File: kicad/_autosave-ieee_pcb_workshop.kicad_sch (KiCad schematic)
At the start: 42 parts, among them J1 Conn_01x10, J2 Conn_01x10, J3 ICSP, J4 USB_B_Micro, U1 ATmega32U4-A, Y1 16MHz

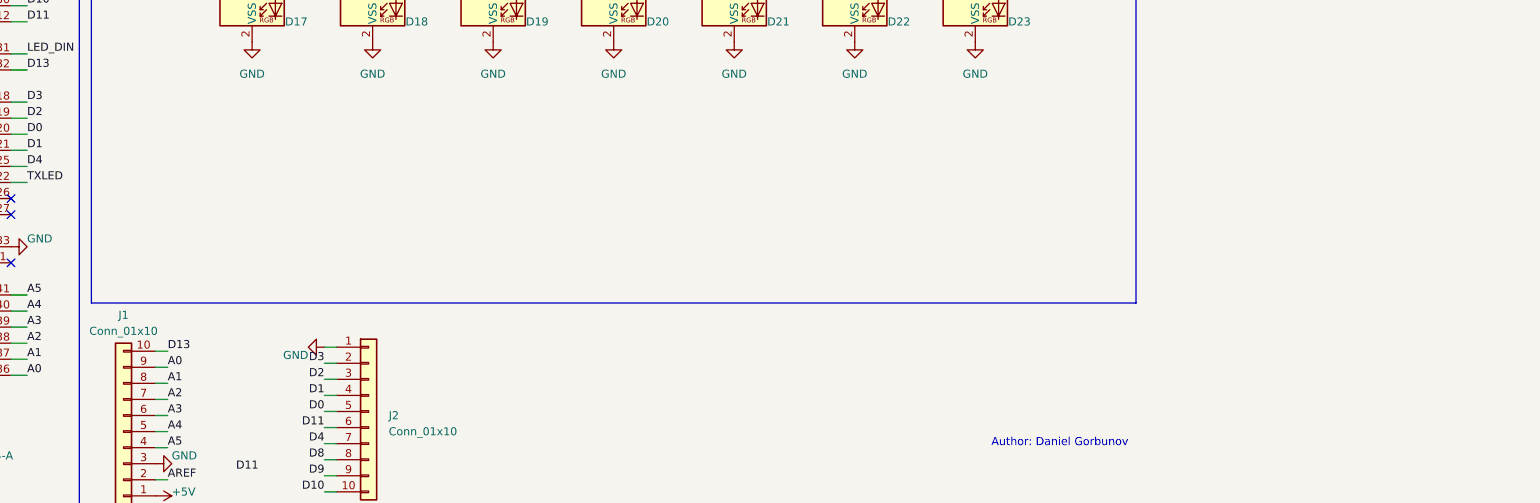
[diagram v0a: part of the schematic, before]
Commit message: add lecture 2
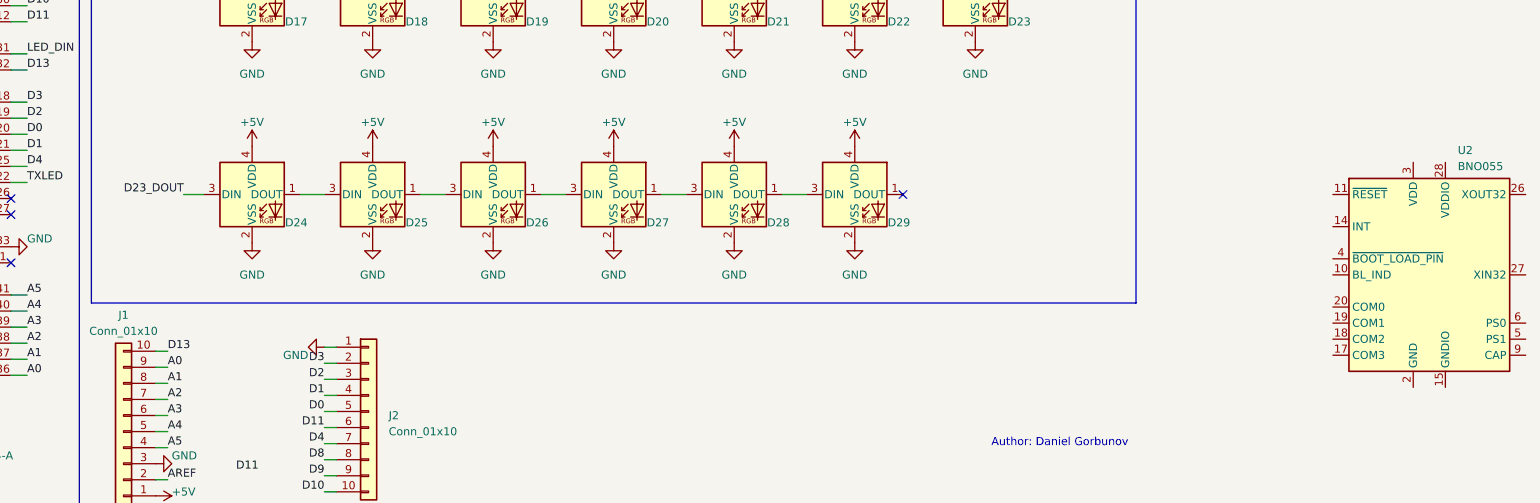
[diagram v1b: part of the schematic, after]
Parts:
- added D24, D25, D26, D27, D28, D29: SK6812MINI, LED_SMD:LED_SK6812MINI_PLCC4_3.5x3.5mm_P1.75mm, symbol LED:SK6812MINI
- added U2: BNO055, Package_LGA:LGA-28_5.2x3.8mm_P0.5mm, symbol Sensor_Motion:BNO055
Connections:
- net +5V: now also D24.4 (VDD), D25.4 (VDD), D26.4 (VDD), D27.4 (VDD), D28.4 (VDD), D29.4 (VDD)
- net D23_DOUT: now also D24.3 (DIN)
- net GND: now also D24.2 (VSS), D25.2 (VSS), D26.2 (VSS), D27.2 (VSS), D28.2 (VSS), D29.2 (VSS)
- new net: D28.1 (DOUT), D29.3 (DIN)
- new net: D25.1 (DOUT), D26.3 (DIN)
- new net: D24.1 (DOUT), D25.3 (DIN)
- new net: U2.15 (GNDIO), U2.16 (GNDIO), U2.25 (GNDIO)
- new net: D27.1 (DOUT), D28.3 (DIN)
- new net: D26.1 (DOUT), D27.3 (DIN)
- no-connect marks 5 -> 6
